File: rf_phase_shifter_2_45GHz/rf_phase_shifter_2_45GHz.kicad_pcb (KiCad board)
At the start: 2 copper layers, 12 parts, among them J1 Conn_Coaxial, J2 Conn_Coaxial, J3 Conn_Coaxial

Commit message: Update rf_phase_shifter_2_45GHz.kicad_pcb
update
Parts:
- moved D1 27.2 mm to (90.9, 78.7), turned to 180 degrees
- moved D3 25.4 mm to (90.9, 87.9), turned to 180 degrees
- moved L1 25.2 mm to (90.7, 83.3), turned to 180 degrees
- moved C1 25.0 mm to (94.0, 92.7), turned to 180 degrees
- moved J2 23.7 mm to (118.6, 92.7), turned to 90 degrees
- moved J3 19.2 mm to (103.4, 103.6)
- moved D4 18.2 mm to (117.3, 78.2)
- moved FL1 14.7 mm to (103.9, 95.0)
- moved J1 8.50 mm to (89.7, 92.7), turned to 270 degrees
- moved D2 7.91 mm to (117.3, 87.9)
- moved C2 6.64 mm to (114.3, 92.7), turned to 180 degrees
- moved L2 3.64 mm to (117.1, 82.8), turned to 180 degrees
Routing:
- net Net-(D2-Pad1): track 0.00 -> 15.9 mm

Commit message: Update rf_phase_shifter_2_45GHz.kicad_pcb
update
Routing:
- net (no net): track 0.00 -> 14.4 mm

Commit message: update
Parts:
- FL1: footprint RF:C2327J5003AHF -> analog_rf_phase_shifter_module:C2327J5003AHF
- moved FL1 1.05 mm to (103.0, 95.5)

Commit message: updated libs
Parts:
- J1, J2, J3: value Conn_Coaxial -> CON-SMA-EDGE-S; footprint Connector_Coaxial:SMA_Samtec_SMA-J-P-X-ST-EM1_EdgeMount -> analog_rf_phase_shifter_module:CON-SMA-EDGE-S
- moved J3 69.6 mm to (122.7, 36.8)
- moved J1 57.8 mm to (104.4, 36.8), turned to 0 degrees
- moved J2 56.1 mm to (113.6, 36.8), turned to 0 degrees
- moved D3 50.6 mm to (64.5, 44.7)
- moved D1 50.6 mm to (64.5, 35.6)
- moved D2 50.6 mm to (90.9, 44.7)
- moved D4 50.6 mm to (90.9, 35.1)
- moved FL1 50.6 mm to (76.5, 52.4)
- moved L1 50.6 mm to (64.2, 40.1)
- moved L2 50.6 mm to (90.6, 39.6)
- moved C1 50.6 mm to (67.5, 49.5)
- moved C2 50.6 mm to (87.8, 49.5)

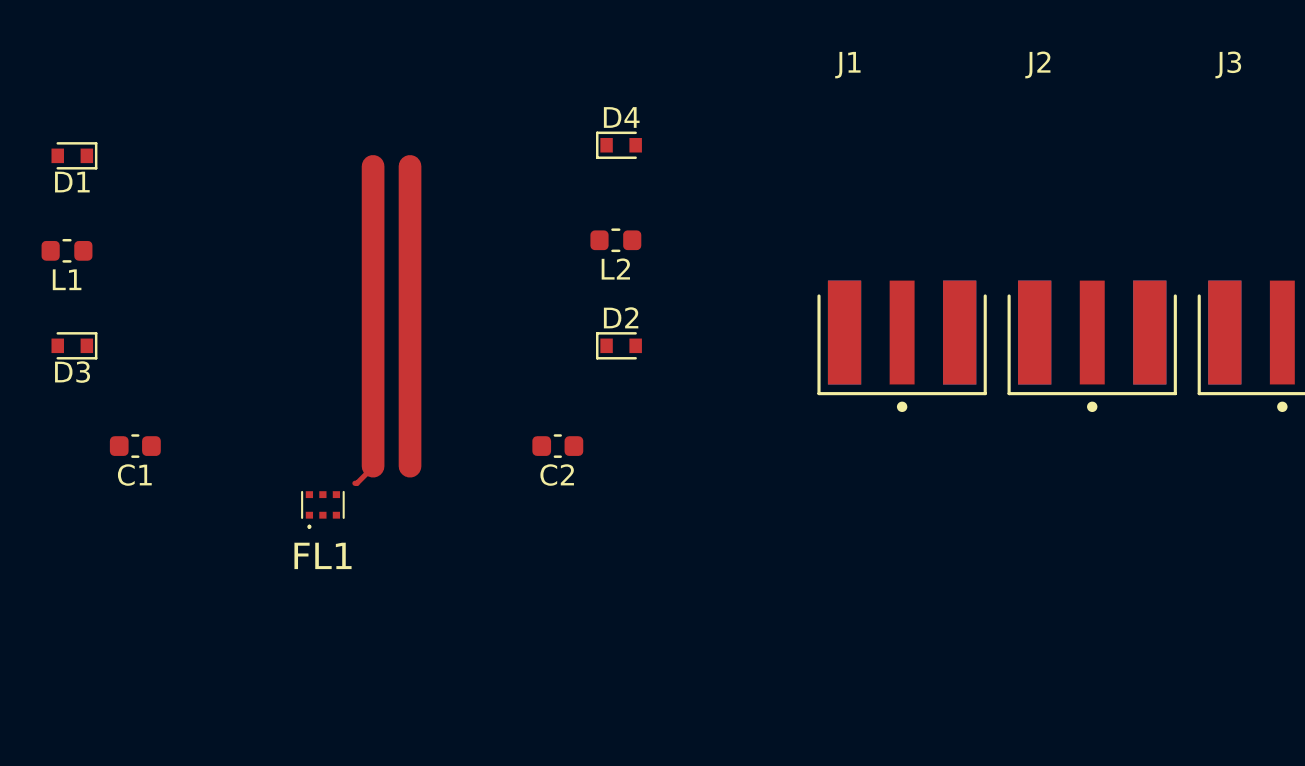
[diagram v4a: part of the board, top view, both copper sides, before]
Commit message: pcb init works
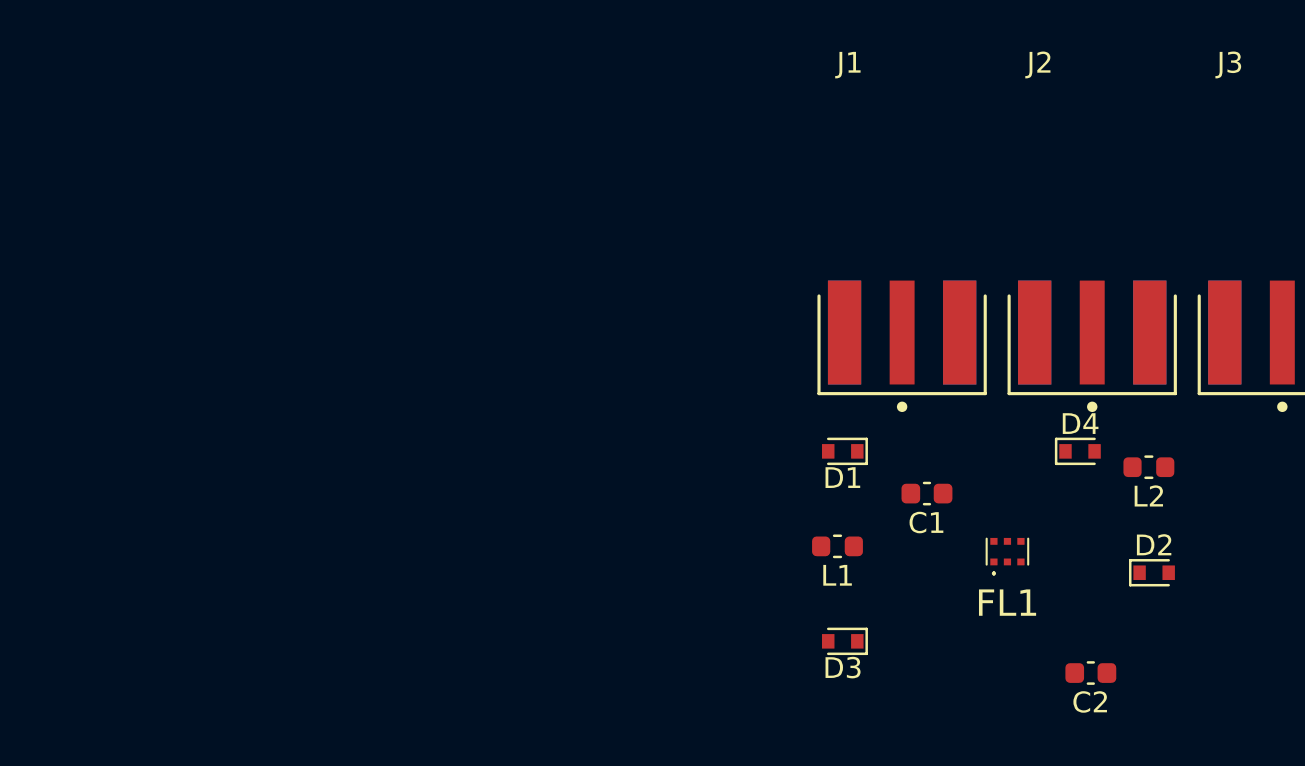
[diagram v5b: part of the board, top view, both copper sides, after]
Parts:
- L1, L2: value 1u -> 220n
- moved D1 39.7 mm to (101.5, 49.8)
- moved D3 39.7 mm to (101.5, 58.9)
- moved L1 39.7 mm to (101.3, 54.4)
- moved C1 38.2 mm to (105.6, 51.8)
- moved FL1 33.0 mm to (109.5, 54.6)
- moved C2 27.9 mm to (113.5, 60.5)
- moved D2 27.9 mm to (116.5, 55.6)
- moved L2 27.9 mm to (116.3, 50.5)
- moved D4 26.5 mm to (113.0, 49.8)
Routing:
- net Net-(D2-Pad1): track 15.6 -> 0.00 mm
- net (no net): track 14.4 -> 0.00 mm
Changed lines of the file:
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@@
     (thickness 1.6)
     (drawings 0)
-    (tracks 5)
+    (tracks 0)
     (zones 0)
     (modules 12)
@@
   )
   (setup
-    (last_trace_width 0.25)
-    (user_trace_width 1.092)
+    (last_trace_width 0.5)
+    (user_trace_width 0.25)
+    (user_trace_width 0.5)
     (trace_clearance 0.2)
     (zone_clearance 0.508)
@@
   )
   (module analog_rf_phase_shifter_module:C2327J5003AHF (layer F.Cu)
-    (at 76.527601 52.362401)
+    (at 109.474 54.61)
     (descr C2327J5003AHF-2)
     (tags Filter)
@@
   )
   (module Inductor_SMD:L_0603_1608Metric (layer F.Cu)
-    (at 90.6272 39.624 180)
+    (at 116.2812 50.546 180)
     (descr "Inductor SMD 0603 (1608 Metric), square (rectangular) end terminal, IPC_7351 nominal, (Body size source: http://www.tortai-tech.com/upload/download/2011102023233369053.pdf), generated with kicad-footprint-generator")
     (tags inductor)
@@
       (effects (font (size 1 1) (thickness 0.15)))
     )
-    (fp_text value 1u (at 0 1.43) (layer F.Fab)
+    (fp_text value 220n (at 0 1.43) (layer F.Fab)
       (effects (font (size 1 1) (thickness 0.15)))
     )
@@
   )
   (module Inductor_SMD:L_0603_1608Metric (layer F.Cu)
-    (at 64.2112 40.132 180)
+    (at 101.2952 54.356 180)
     (descr "Inductor SMD 0603 (1608 Metric), square (rectangular) end terminal, IPC_7351 nominal, (Body size source: http://www.tortai-tech.com/upload/download/2011102023233369053.pdf), generated with kicad-footprint-generator")
     (tags inductor)
@@
       (effects (font (size 1 1) (thickness 0.15)))
     )
-    (fp_text value 1u (at 0 1.43) (layer F.Fab)
+    (fp_text value 220n (at 0 1.43) (layer F.Fab)
       (effects (font (size 1 1) (thickness 0.15)))
     )
@@
   )
   (module Diode_SMD:D_SOD-523 (layer F.Cu)
-    (at 90.8812 35.052)
+    (at 112.968 49.784)
     (descr "http://www.diodes.com/datasheets/ap02001.pdf p.144")
     (tags "Diode SOD523")
@@
   )
   (module Diode_SMD:D_SOD-523 (layer F.Cu)
-    (at 64.4652 44.704 180)
+    (at 101.5492 58.928 180)
     (descr "http://www.diodes.com/datasheets/ap02001.pdf p.144")
     (tags "Diode SOD523")
@@
   )
   (module Diode_SMD:D_SOD-523 (layer F.Cu)
-    (at 90.8812 44.704)
+    (at 116.5352 55.626)
     (descr "http://www.diodes.com/datasheets/ap02001.pdf p.144")
     (tags "Diode SOD523")
@@
   )
   (module Diode_SMD:D_SOD-523 (layer F.Cu)
-    (at 64.4652 35.56 180)
+    (at 101.5492 49.784 180)
     (descr "http://www.diodes.com/datasheets/ap02001.pdf p.144")
     (tags "Diode SOD523")
@@
   )
   (module Capacitor_SMD:C_0603_1608Metric (layer F.Cu)
-    (at 87.8332 49.53 180)
+    (at 113.4872 60.452 180)
     (descr "Capacitor SMD 0603 (1608 Metric), square (rectangular) end terminal, IPC_7351 nominal, (Body size source: IPC-SM-782 page 76, https://www.pcb-3d.com/wordpress/wp-content/uploads/ipc-sm-782a_amendment_1_and_2.pdf), generated with kicad-footprint-generator")
     (tags capacitor)
@@
   )
   (module Capacitor_SMD:C_0603_1608Metric (layer F.Cu)
-    (at 67.5002 49.53 180)
+    (at 105.6002 51.816 180)
     (descr "Capacitor SMD 0603 (1608 Metric), square (rectangular) end terminal, IPC_7351 nominal, (Body size source: IPC-SM-782 page 76, https://www.pcb-3d.com/wordpress/wp-content/uploads/ipc-sm-782a_amendment_1_and_2.pdf), generated with kicad-footprint-generator")
     (tags capacitor)
@@
     )
   )
-  (segment (start 80.7212 50.498) (end 80.7212 36.068) (width 1.092) (layer F.Cu) (net 0))
-  (segment (start 78.0692 51.321) (end 78.1682 51.321) (width 0.25) (layer F.Cu) (net 7))
-  (segment (start 78.9432 50.498) (end 78.9432 36.068) (width 1.092) (layer F.Cu) (net 7))
-  (segment (start 78.1682 51.321) (end 78.8162 50.673) (width 0.25) (layer F.Cu) (net 7))
-  (segment (start 78.8162 50.673) (end 78.9432 50.546) (width 0.25) (layer F.Cu) (net 7))
 )

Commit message: finished pcb layouts
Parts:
- added TL1: TL_13_2_45GHz, analog_rf_phase_shifter_module:TL_13_2_45GHz, F.Cu at (94.1, 57.3)
- added TL2: TL_13_2_45GHz, analog_rf_phase_shifter_module:TL_13_2_45GHz, F.Cu at (94.1, 60.6)
- added TL3: TL_24_2_45GHz, analog_rf_phase_shifter_module:TL_24_2_45GHz, F.Cu at (110.7, 57.3)
- added TL4: TL_24_2_45GHz, analog_rf_phase_shifter_module:TL_24_2_45GHz, F.Cu at (110.7, 60.6)
- moved J3 58.4 mm to (68.7, 58.9), turned to 90 degrees
- moved J2 47.2 mm to (84.5, 73.9), turned to 180 degrees
- moved L2 32.0 mm to (86.5, 62.2), turned to 90 degrees
- moved C2 29.1 mm to (84.5, 62.2), turned to 90 degrees
- moved FL1 24.3 mm to (85.6, 58.9), turned to 270 degrees
- moved C1 21.5 mm to (84.5, 55.6), turned to 90 degrees
- moved J1 21.2 mm to (84.5, 43.9)
- moved D3 17.8 mm to (119.2, 56.6), turned to 90 degrees
- moved D2 15.6 mm to (102.2, 61.7), turned to 270 degrees
- moved L1 14.9 mm to (86.5, 55.6), turned to 270 degrees
- moved D4 13.1 mm to (119.2, 61.3), turned to 270 degrees
- moved D1 6.38 mm to (102.2, 56.1), turned to 90 degrees
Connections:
- D3 pad 1: Net-(D1-Pad1) -> Net-(D3-Pad1)
- D4 pad 1: Net-(D2-Pad1) -> Net-(D4-Pad1)
- FL1 pad 4: Net-(D2-Pad1) -> Net-(FL1-Pad4)
- FL1 pad 6: Net-(D1-Pad1) -> Net-(FL1-Pad6)
- L1 pad 2: Net-(D1-Pad1) -> Net-(FL1-Pad6)
- L2 pad 2: Net-(D2-Pad1) -> Net-(FL1-Pad4)
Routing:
- net GND: track 0.00 -> 69.4 mm, vias 0 -> 31
- net Net-(D2-Pad1): track 0.00 -> 46.8 mm
- net Net-(J3-Pad1): track 0.00 -> 30.7 mm, vias 0 -> 4
- net Net-(D1-Pad1): track 0.00 -> 30.5 mm
- net Net-(FL1-Pad4): track 0.00 -> 9.93 mm
- net Net-(D4-Pad1): track 0.00 -> 8.48 mm
- net Net-(FL1-Pad6): track 0.00 -> 6.22 mm
- net Net-(D3-Pad1): track 0.00 -> 4.75 mm
- net Net-(C1-Pad2): track 0.00 -> 3.65 mm
- net Net-(C2-Pad1): track 0.00 -> 3.65 mm
- net Net-(C2-Pad2): track 0.00 -> 1.67 mm
- net Net-(C1-Pad1): track 0.00 -> 1.67 mm
- added copper zone on B.Cu, net GND
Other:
- board outline added: 53.5 x 21 mm
- board text added: "Analog RF phase shifter 2.45GHz Marcin Wachowiak, Poland"
- board text added: "BIAS"
- board text added: "IN"
- board text added: "OUT"
